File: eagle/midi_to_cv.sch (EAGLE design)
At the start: 76 parts, among them IC1 TL084P, IC2 TL084P, IC3 TL084P, IC4 TL084P, IC5 TL084P, U1 ATMEGA328P_PDIP

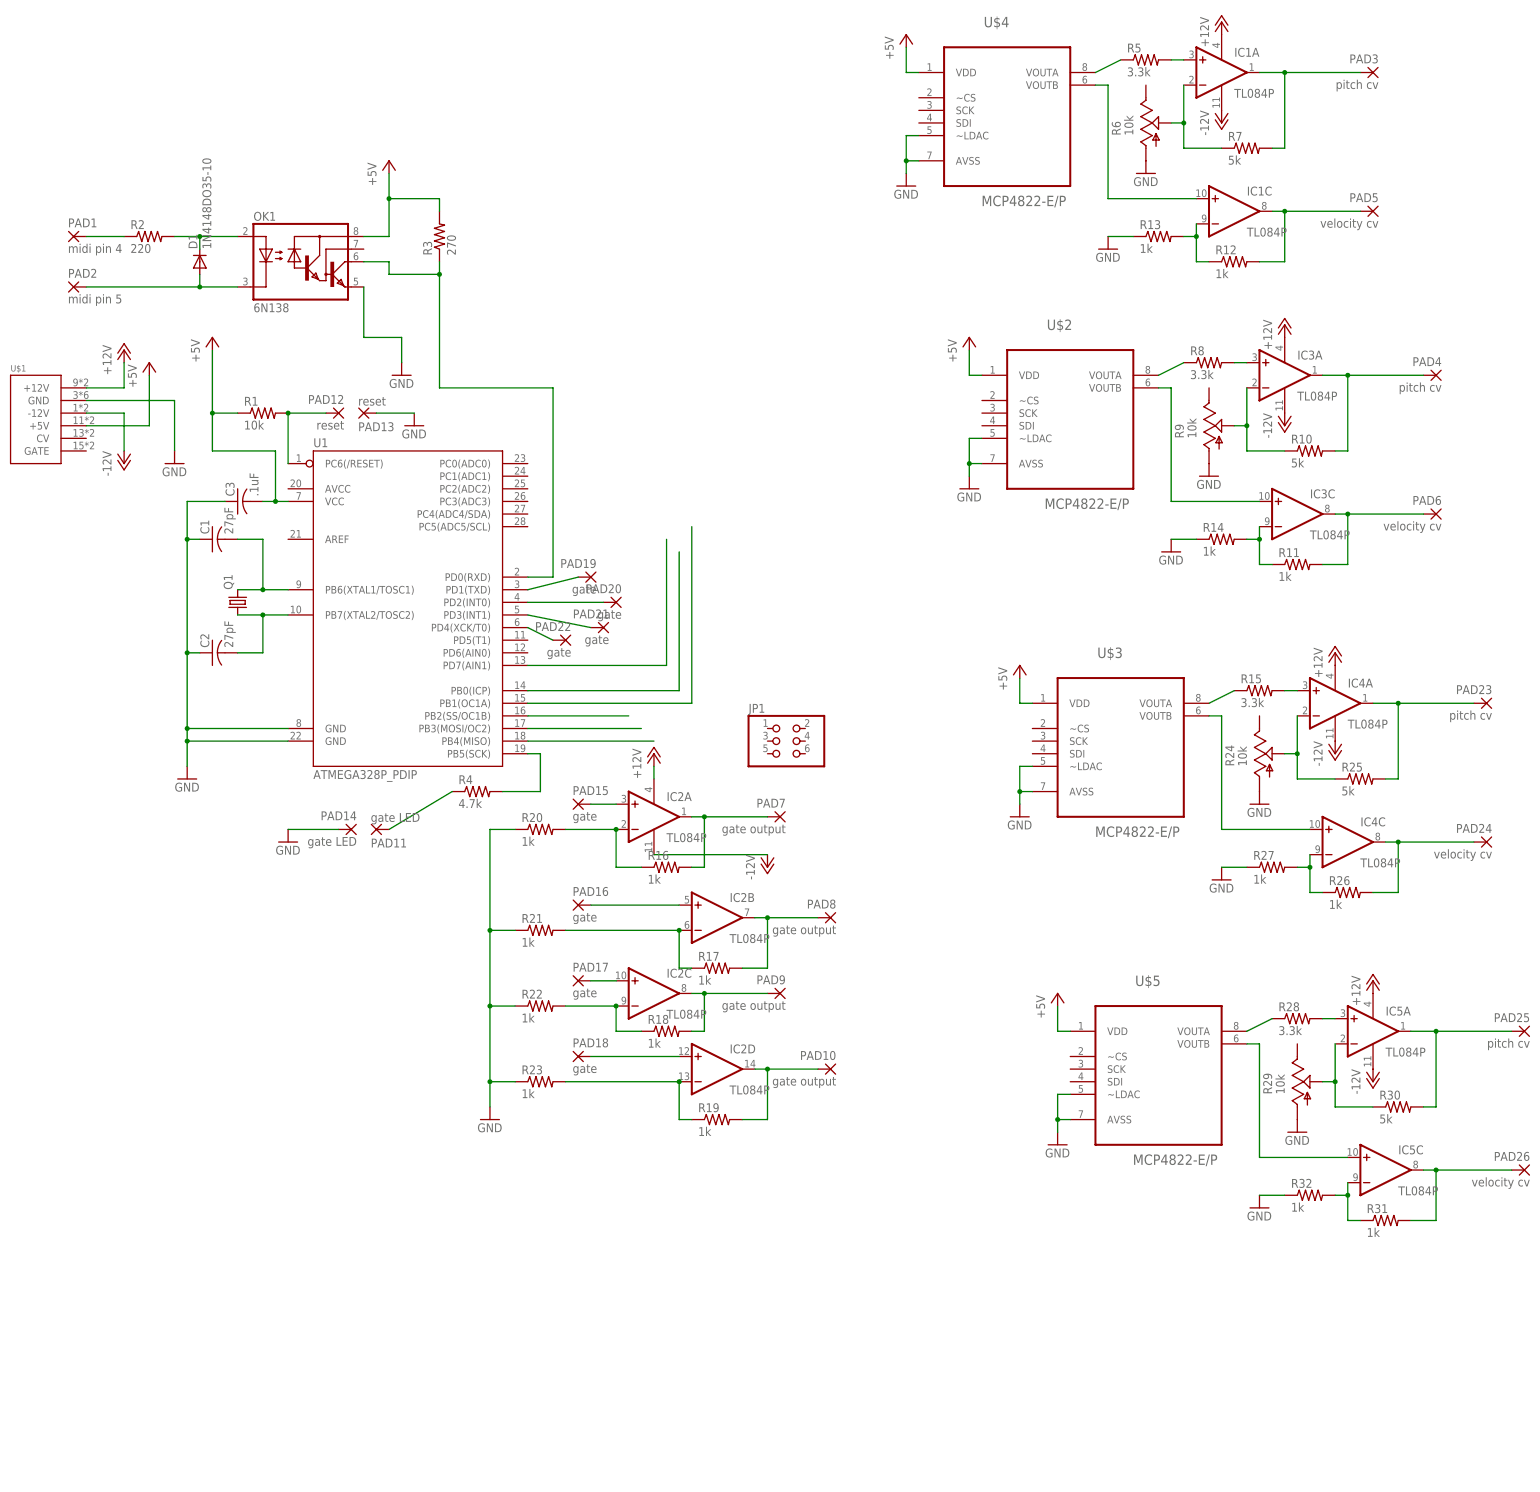
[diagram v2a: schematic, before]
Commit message: connected the dacs
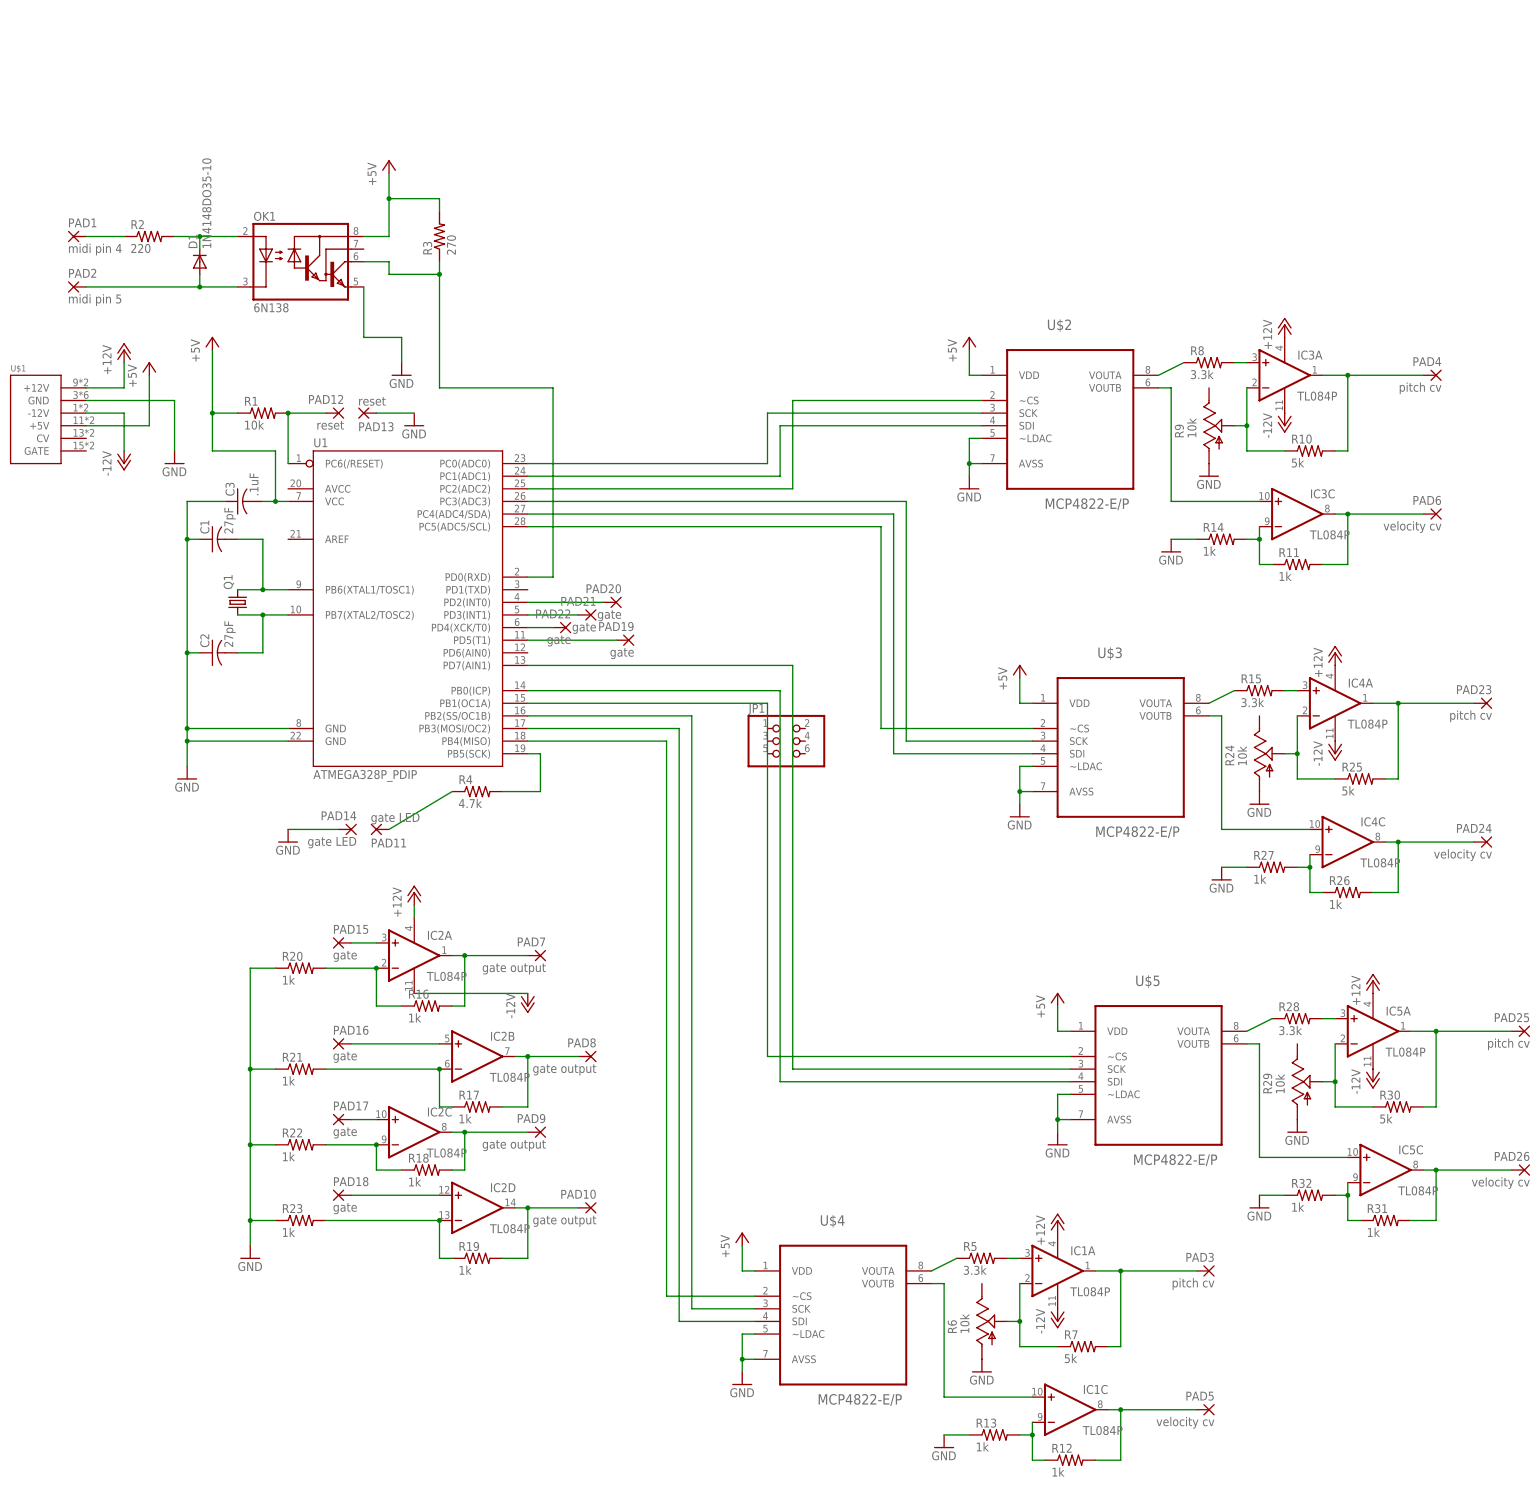
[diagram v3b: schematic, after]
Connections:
- new net N$62: U$2.SCK, U1.PC0(ADC0)
- new net N$63: U$2.SDI, U1.PC1(ADC1)
- new net N$64: U$2.~CS, U1.PC2(ADC2)
- new net N$65: U$3.SCK, U1.PC3(ADC3)
- new net N$66: U$3.SDI, U1.PC4(ADC4/SDA)
- new net N$67: U$3.~CS, U1.PC5(ADC5/SCL)
- net N$14: now also U$4.SDI
- net N$15: now also U$4.SCK
- net N$23: now also U$5.SDI
- net N$27: now also U$4.~CS
- net N$28: now also U$5.SCK
- net N$29: now also U$5.~CS
- net N$31: now also U1.PD5(T1); no longer U1.PD1(TXD)
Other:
- moved on the sheet: IC1A, IC1C, IC2A, IC2B, IC2C, IC2D, PAD10, PAD15, PAD16, PAD17, PAD18, PAD19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

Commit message: prettied up the schematic
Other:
- moved on the sheet: IC1A, IC1C, IC3A, IC3C, IC4A, IC4C, IC5A, IC5C, PAD23, PAD24, PAD25, PAD26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

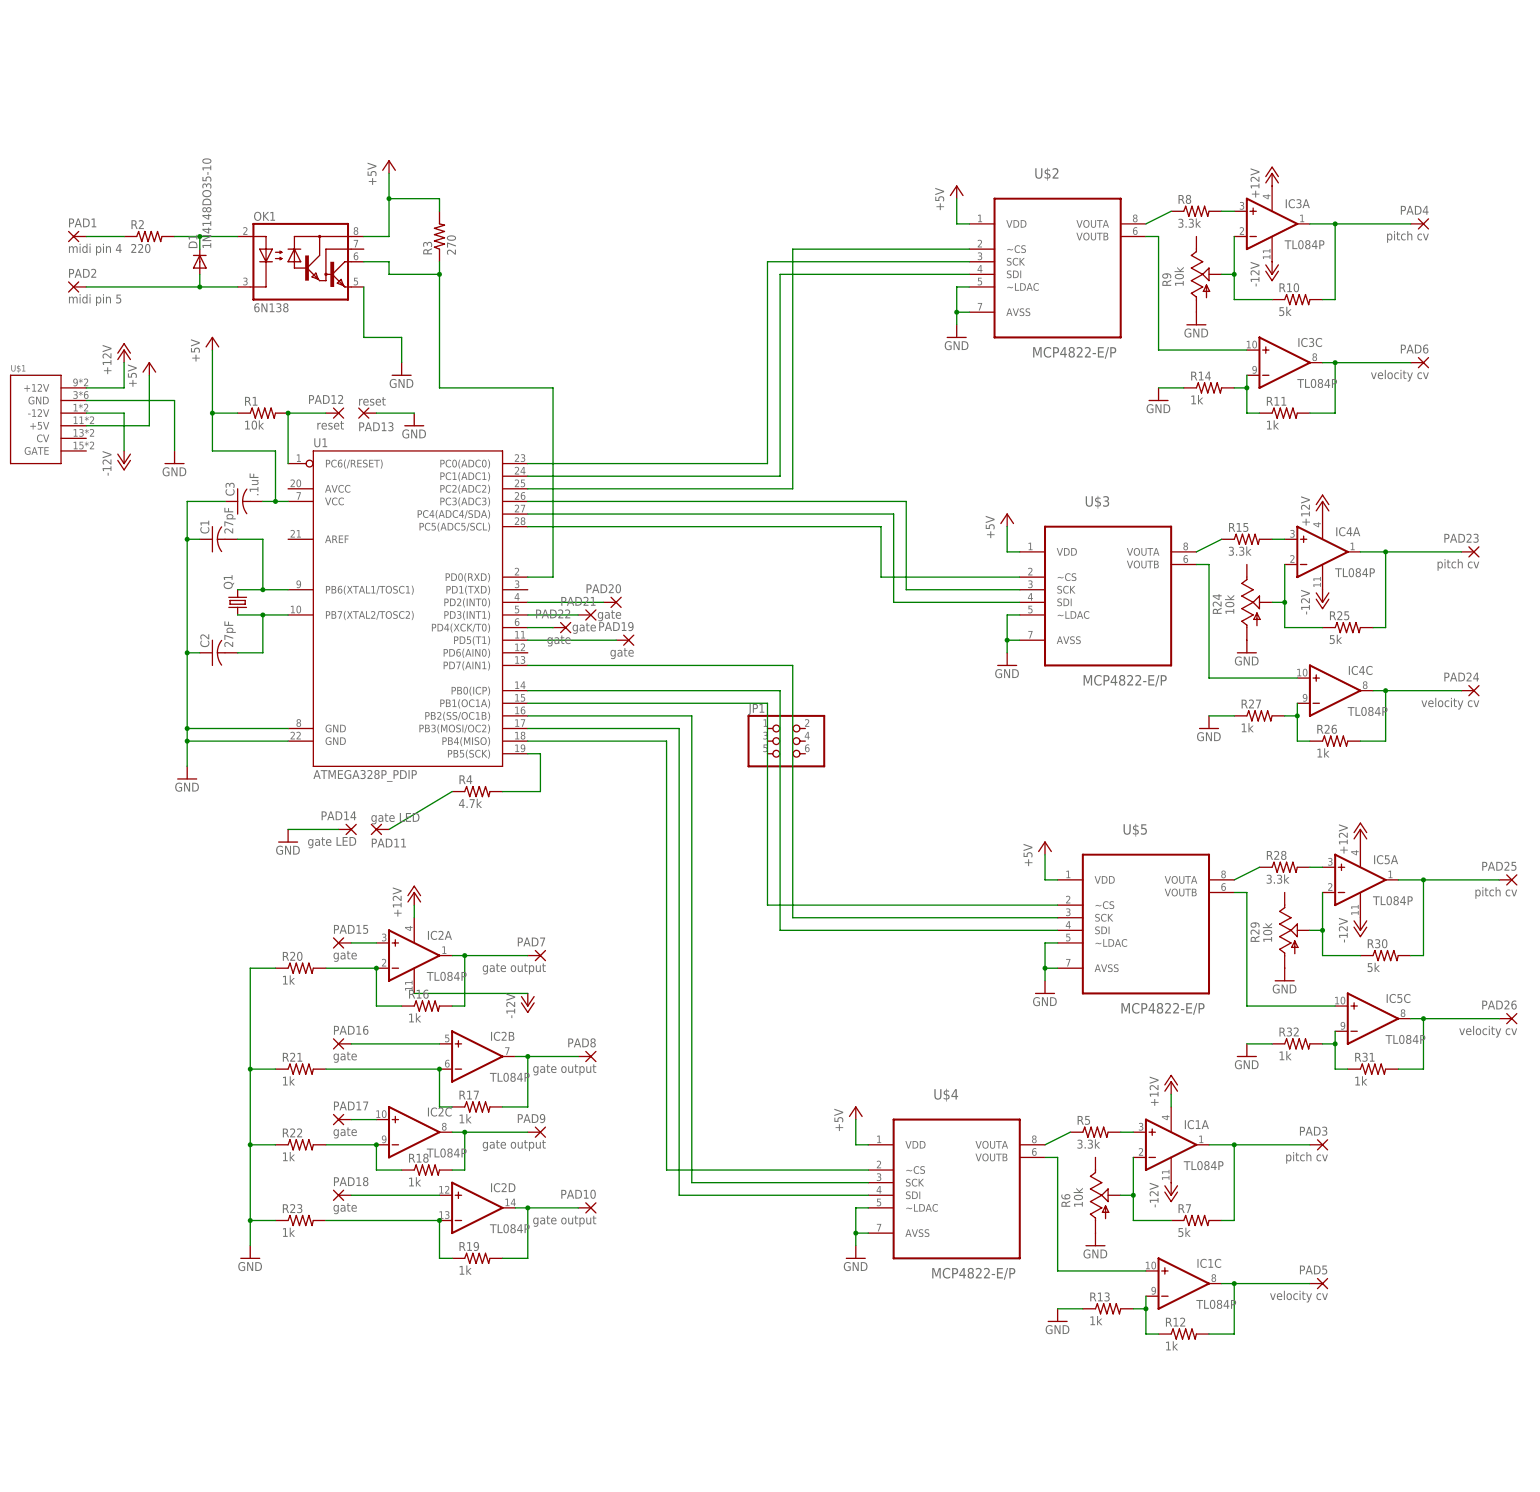
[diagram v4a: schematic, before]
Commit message: renumbered op amps
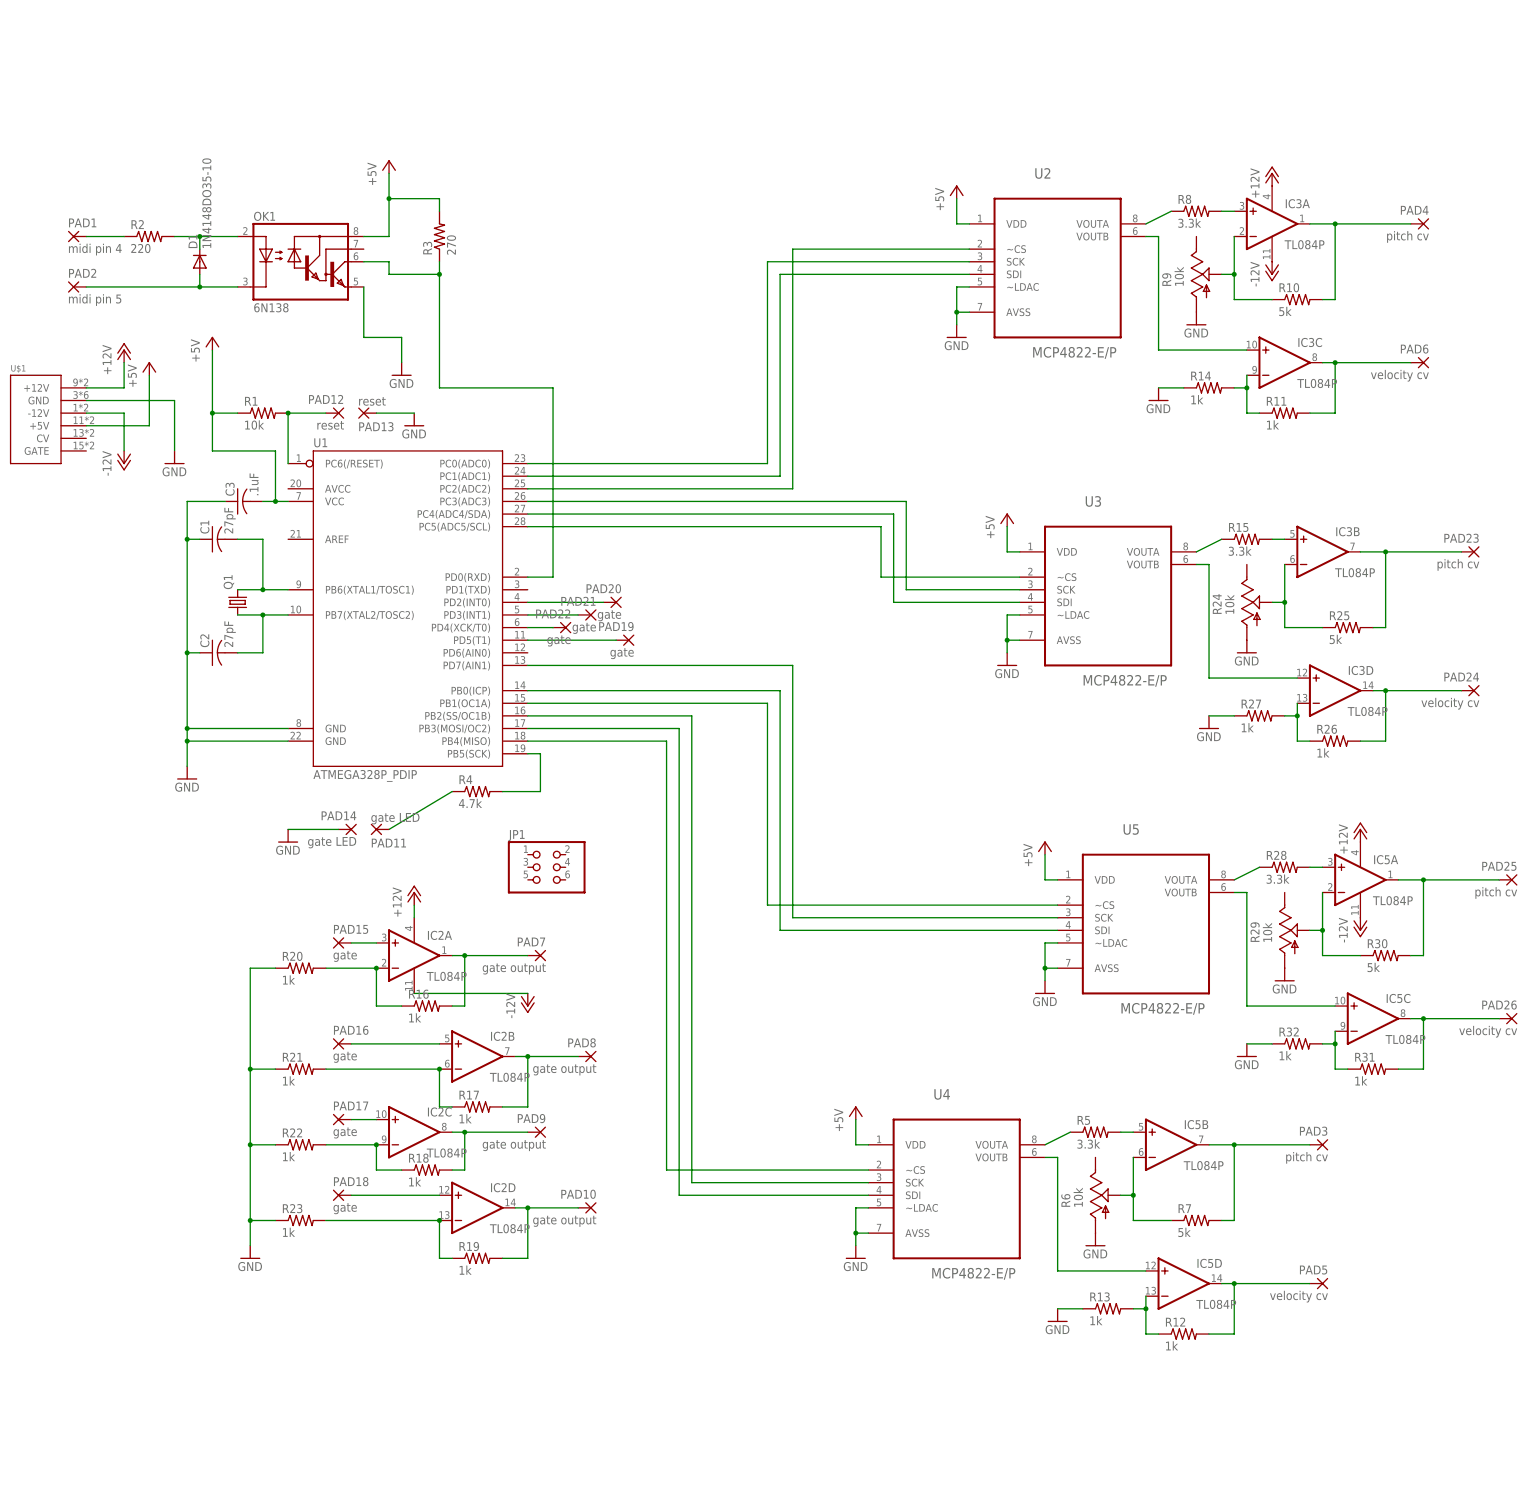
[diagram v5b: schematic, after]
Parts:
- removed IC1, IC4: TL084P, linear:TL084P
- renumbered U$2 to U2, U$3 to U3, U$4 to U4, U$5 to U5
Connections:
- net +12V: no longer IC1P.V+, IC4P.V+
- net -12V: no longer IC1P.V-, IC4P.V-
- net N$12: now also IC5B.-IN; no longer IC1A.-IN
- net N$19: now also IC5D.OUT; no longer IC1C.OUT
- net N$20: now also IC5D.-IN; no longer IC1C.-IN
- net N$26: now also IC3B.+IN; no longer IC4A.+IN
- net N$49: now also IC3B.OUT; no longer IC4A.OUT
- net N$50: now also IC3B.-IN; no longer IC4A.-IN
- net N$51: now also IC5D.+IN; no longer IC1C.+IN
- net N$52: now also IC3D.OUT; no longer IC4C.OUT
- net N$53: now also IC3D.-IN; no longer IC4C.-IN
- net N$54: now also IC3D.+IN; no longer IC4C.+IN
- net N$6: now also IC5B.+IN; no longer IC1A.+IN
- net N$9: now also IC5B.OUT; no longer IC1A.OUT
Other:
- moved on the sheet: JP1
